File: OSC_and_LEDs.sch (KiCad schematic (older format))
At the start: 49 parts, among them Q2 IRLML2502, Q3 IRLML2502, Q4 IRLML2502, Q5 IRLML2502, Q6 IRLML2502, Q7 IRLML2502, U1 xc7a50tftg256, X1 ASFLMB

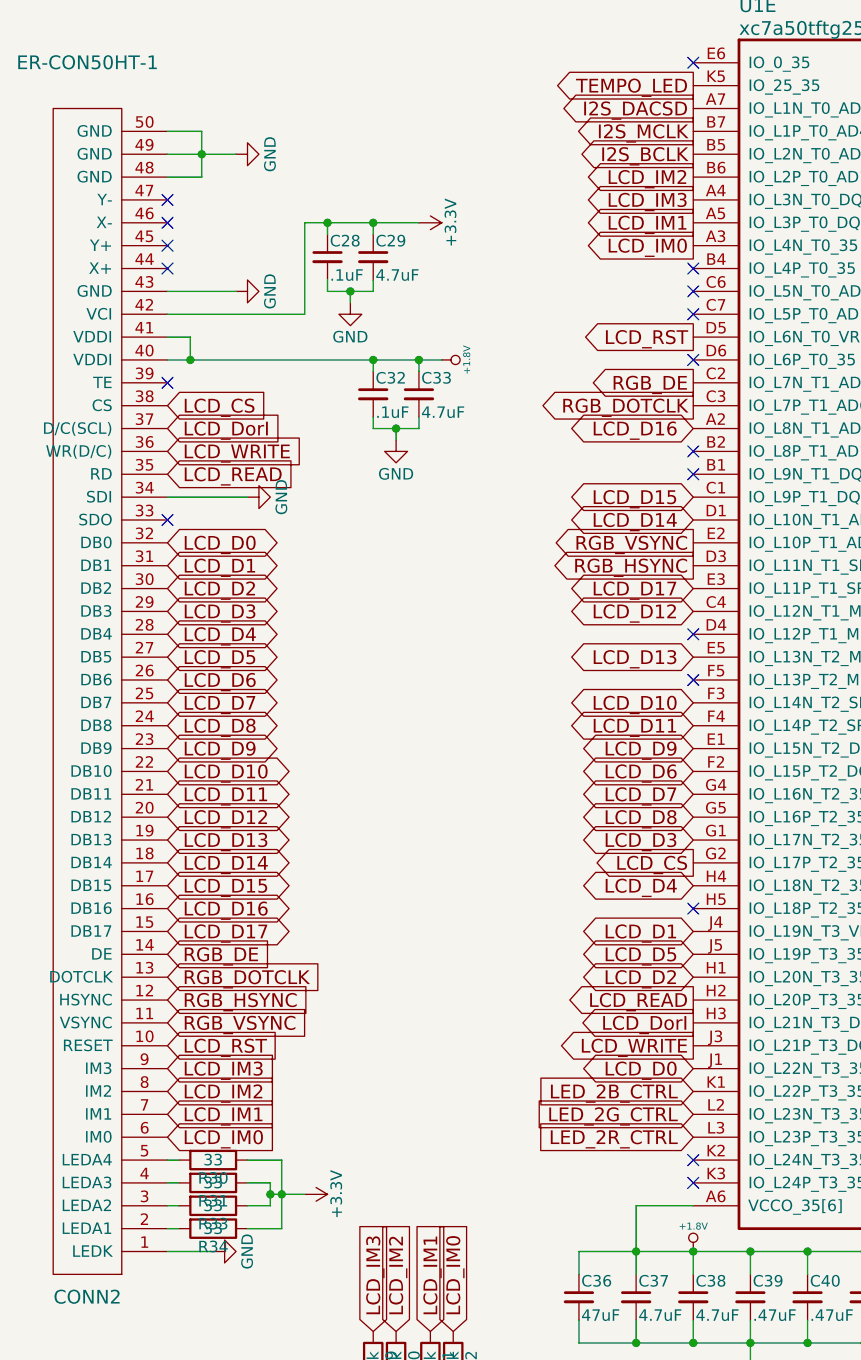
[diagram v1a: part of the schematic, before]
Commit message: all high speed busses added
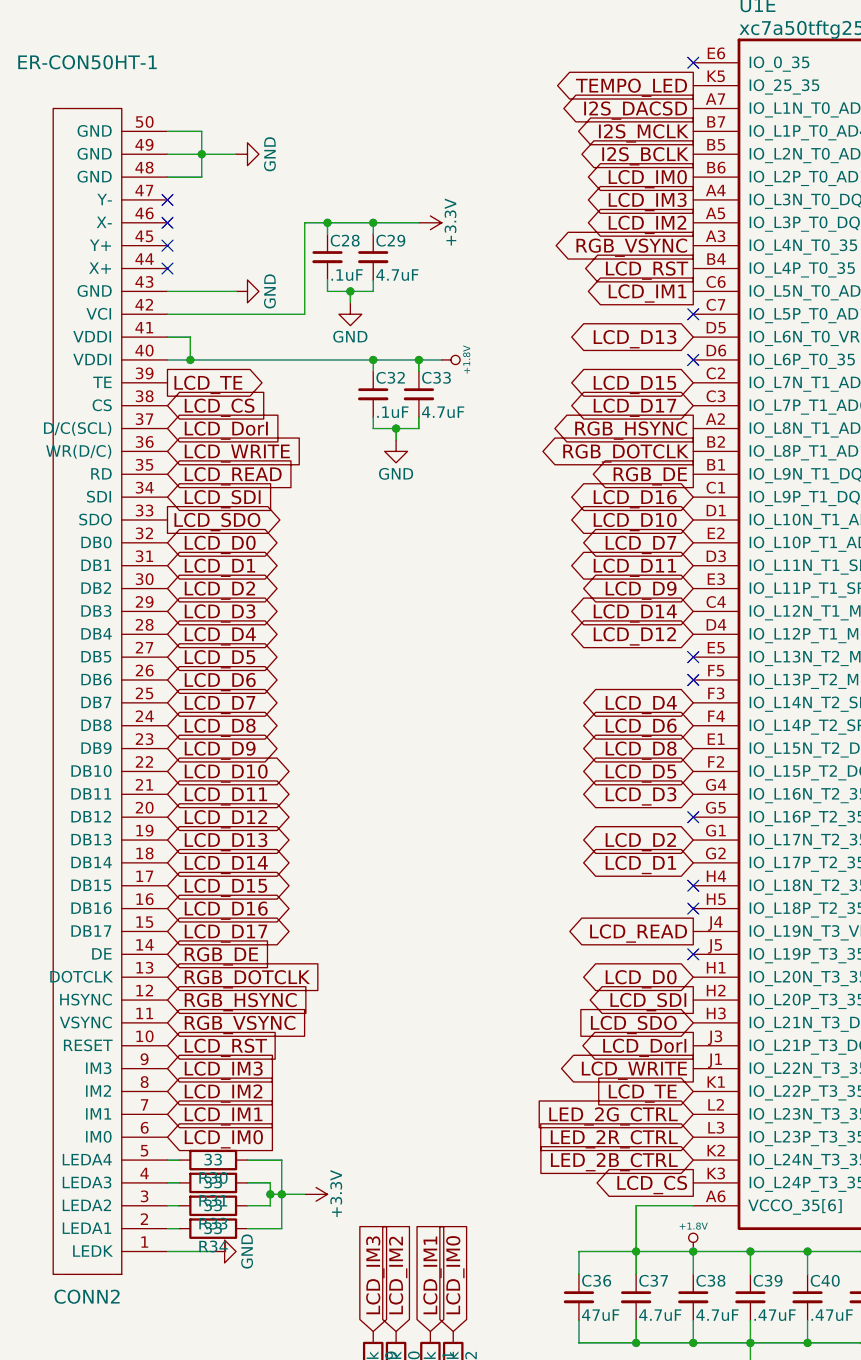
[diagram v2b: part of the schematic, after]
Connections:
- net GND: no longer CONN2.34 (SDI)
- net LCD_CS: now also U1.K3 (IO_L24P_T3_35); no longer U1.G2 (IO_L17P_T2_35)
- net LCD_D0: now also U1.H1 (IO_L20N_T3_35); no longer U1.J1 (IO_L22N_T3_35)
- net LCD_D1: now also U1.G2 (IO_L17P_T2_35); no longer U1.J4 (IO_L19N_T3_VREF_35)
- net LCD_D10: now also U1.D1 (IO_L10N_T1_AD15N_35); no longer U1.F3 (IO_L14N_T2_SRCC_35)
- net LCD_D11: now also U1.D3 (IO_L11N_T1_SRCC_35); no longer U1.F4 (IO_L14P_T2_SRCC_35)
- net LCD_D12: now also U1.D4 (IO_L12P_T1_MRCC_35); no longer U1.C4 (IO_L12N_T1_MRCC_35)
- net LCD_D13: now also U1.D5 (IO_L6N_T0_VREF_35); no longer U1.E5 (IO_L13N_T2_MRCC_35)
- net LCD_D14: now also U1.C4 (IO_L12N_T1_MRCC_35); no longer U1.D1 (IO_L10N_T1_AD15N_35)
- net LCD_D15: now also U1.C2 (IO_L7N_T1_AD6N_35); no longer U1.C1 (IO_L9P_T1_DQS_AD7P_35)
- net LCD_D16: now also U1.C1 (IO_L9P_T1_DQS_AD7P_35); no longer U1.A2 (IO_L8N_T1_AD14N_35)
- net LCD_D17: now also U1.C3 (IO_L7P_T1_AD6P_35); no longer U1.E3 (IO_L11P_T1_SRCC_35)
- net LCD_D2: now also U1.G1 (IO_L17N_T2_35); no longer U1.H1 (IO_L20N_T3_35)
- net LCD_D3: now also U1.G4 (IO_L16N_T2_35); no longer U1.G1 (IO_L17N_T2_35)
- net LCD_D4: now also U1.F3 (IO_L14N_T2_SRCC_35); no longer U1.H4 (IO_L18N_T2_35)
- net LCD_D5: now also U1.F2 (IO_L15P_T2_DQS_35); no longer U1.J5 (IO_L19P_T3_35)
- net LCD_D6: now also U1.F4 (IO_L14P_T2_SRCC_35); no longer U1.F2 (IO_L15P_T2_DQS_35)
- net LCD_D7: now also U1.E2 (IO_L10P_T1_AD15P_35); no longer U1.G4 (IO_L16N_T2_35)
- net LCD_D8: now also U1.E1 (IO_L15N_T2_DQS_35); no longer U1.G5 (IO_L16P_T2_35)
- net LCD_D9: now also U1.E3 (IO_L11P_T1_SRCC_35); no longer U1.E1 (IO_L15N_T2_DQS_35)
- net LCD_DorI: now also U1.J3 (IO_L21P_T3_DQS_35); no longer U1.H3 (IO_L21N_T3_DQS_35)
- net LCD_IM0: now also U1.B6 (IO_L2P_T0_AD12P_35); no longer U1.A3 (IO_L4N_T0_35)
- net LCD_IM1: now also U1.C6 (IO_L5N_T0_AD13N_35); no longer U1.A5 (IO_L3P_T0_DQS_AD5P_35)
- net LCD_IM2: now also U1.A5 (IO_L3P_T0_DQS_AD5P_35); no longer U1.B6 (IO_L2P_T0_AD12P_35)
- net LCD_READ: now also U1.J4 (IO_L19N_T3_VREF_35); no longer U1.H2 (IO_L20P_T3_35)
- net LCD_RST: now also U1.B4 (IO_L4P_T0_35); no longer U1.D5 (IO_L6N_T0_VREF_35)
- net LCD_WRITE: now also U1.J1 (IO_L22N_T3_35); no longer U1.J3 (IO_L21P_T3_DQS_35)
- net LED_2B_CTRL: now also U1.K2 (IO_L24N_T3_35); no longer U1.K1 (IO_L22P_T3_35)
- net RGB_DE: now also U1.B1 (IO_L9N_T1_DQS_AD7N_35); no longer U1.C2 (IO_L7N_T1_AD6N_35)
- net RGB_DOTCLK: now also U1.B2 (IO_L8P_T1_AD14P_35); no longer U1.C3 (IO_L7P_T1_AD6P_35)
- net RGB_HSYNC: now also U1.A2 (IO_L8N_T1_AD14N_35); no longer U1.D3 (IO_L11N_T1_SRCC_35)
- net RGB_VSYNC: now also U1.A3 (IO_L4N_T0_35); no longer U1.E2 (IO_L10P_T1_AD15P_35)
- net LCD_SDO: now reaches CONN2.33 (SDO)
- net LCD_SDO: now also U1.H3 (IO_L21N_T3_DQS_35)
- net LCD_TE: now reaches CONN2.39 (TE)
- net LCD_TE: now also U1.K1 (IO_L22P_T3_35)
- new net LCD_SDI: CONN2.34 (SDI), U1.H2 (IO_L20P_T3_35)
- no-connect marks 30 -> 25
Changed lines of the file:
@@
-$EndComp
-$Comp
-L GND #PWR053
-U 1 1 598D5E39
-P 7650 2800
-F 0 "#PWR053" H 7650 2550 50  0001 C CNN
-F 1 "GND" H 7650 2650 50  0000 C CNN
-F 2 "" H 7650 2800 50  0000 C CNN
-F 3 "" H 7650 2800 50  0000 C CNN
-	1    7650 2800
-	0    -1   -1   0
 $EndComp
 $Comp
@@
 $EndComp
 $Comp
-L GND #PWR054
+L GND #PWR053
 U 1 1 598F040F
 P 4750 1600
-F 0 "#PWR054" H 4750 1350 50  0001 C CNN
+F 0 "#PWR053" H 4750 1350 50  0001 C CNN
 F 1 "GND" H 4750 1450 50  0000 C CNN
 F 2 "" H 4750 1600 50  0000 C CNN
@@
 $EndComp
 $Comp
-L +3.3V #PWR055
+L +3.3V #PWR054
 U 1 1 598F1F44
 P 4300 2100
-F 0 "#PWR055" H 4300 1950 50  0001 C CNN
+F 0 "#PWR054" H 4300 1950 50  0001 C CNN
 F 1 "+3.3V" H 4300 2240 50  0000 C CNN
 F 2 "" H 4300 2100 50  0000 C CNN
@@
 $EndComp
 $Comp
-L GND #PWR056
+L GND #PWR055
 U 1 1 598FDD2A
 P 4500 2600
-F 0 "#PWR056" H 4500 2350 50  0001 C CNN
+F 0 "#PWR055" H 4500 2350 50  0001 C CNN
 F 1 "GND" H 4500 2450 50  0000 C CNN
 F 2 "" H 4500 2600 50  0000 C CNN
@@
 $EndComp
 $Comp
-L GND #PWR057
+L GND #PWR056
 U 1 1 598D6E85
 P 2550 4500
-F 0 "#PWR057" H 2550 4250 50  0001 C CNN
+F 0 "#PWR056" H 2550 4250 50  0001 C CNN
 F 1 "GND" H 2550 4350 50  0000 C CNN
 F 2 "" H 2550 4500 50  0000 C CNN
@@
 $EndComp
 $Comp
-L GND #PWR058
+L GND #PWR057
 U 1 1 598D6E8B
 P 2550 4000
-F 0 "#PWR058" H 2550 3750 50  0001 C CNN
+F 0 "#PWR057" H 2550 3750 50  0001 C CNN
 F 1 "GND" H 2550 3850 50  0000 C CNN
 F 2 "" H 2550 4000 50  0000 C CNN
@@
 $EndComp
 $Comp
-L GND #PWR059
+L GND #PWR058
 U 1 1 598D6E97
 P 2550 3700
-F 0 "#PWR059" H 2550 3450 50  0001 C CNN
+F 0 "#PWR058" H 2550 3450 50  0001 C CNN
 F 1 "GND" H 2550 3550 50  0000 C CNN
 F 2 "" H 2550 3700 50  0000 C CNN
@@
 $EndComp
 $Comp
-L GND #PWR060
+L GND #PWR059
 U 1 1 598D6E9D
 P 2550 3600
-F 0 "#PWR060" H 2550 3350 50  0001 C CNN
+F 0 "#PWR059" H 2550 3350 50  0001 C CNN
 F 1 "GND" H 2550 3450 50  0000 C CNN
 F 2 "" H 2550 3600 50  0000 C CNN
@@
 $EndComp
 $Comp
-L GND #PWR061
+L GND #PWR060
 U 1 1 598D6EA3
 P 2550 3300
-F 0 "#PWR061" H 2550 3050 50  0001 C CNN
+F 0 "#PWR060" H 2550 3050 50  0001 C CNN
 F 1 "GND" H 2550 3150 50  0000 C CNN
 F 2 "" H 2550 3300 50  0000 C CNN
@@
 $EndComp
 $Comp
-L GND #PWR062
+L GND #PWR061
 U 1 1 598D6EA9
 P 2550 3000
-F 0 "#PWR062" H 2550 2750 50  0001 C CNN
+F 0 "#PWR061" H 2550 2750 50  0001 C CNN
 F 1 "GND" H 2550 2850 50  0000 C CNN
 F 2 "" H 2550 3000 50  0000 C CNN
@@
 $EndComp
 $Comp
-L GND #PWR063
+L GND #PWR062
 U 1 1 598D6EAF
 P 2550 2700
-F 0 "#PWR063" H 2550 2450 50  0001 C CNN
+F 0 "#PWR062" H 2550 2450 50  0001 C CNN
 F 1 "GND" H 2550 2550 50  0000 C CNN
 F 2 "" H 2550 2700 50  0000 C CNN
@@
 $EndComp
 $Comp
-L GND #PWR064
+L GND #PWR063
 U 1 1 598D6EB7
 P 2550 2800
-F 0 "#PWR064" H 2550 2550 50  0001 C CNN
+F 0 "#PWR063" H 2550 2550 50  0001 C CNN
 F 1 "GND" H 2550 2650 50  0000 C CNN
 F 2 "" H 2550 2800 50  0000 C CNN
@@
 $EndComp
 $Comp
-L +1.8V #PWR065
+L +1.8V #PWR064
 U 1 1 598CFD34
 P 8500 6900
-F 0 "#PWR065" H 8500 7040 20  0001 C CNN
+F 0 "#PWR064" H 8500 7040 20  0001 C CNN
 F 1 "+1.8V" H 8500 7010 30  0000 C CNN
 F 2 "" H 8500 6900 60  0001 C CNN
@@
 $EndComp
 $Comp
-L GND #PWR066
+L GND #PWR065
 U 1 1 598D049B
 P 8250 6900
-F 0 "#PWR066" H 8250 6650 50  0001 C CNN
+F 0 "#PWR065" H 8250 6650 50  0001 C CNN
 F 1 "GND" H 8250 6750 50  0000 C CNN
 F 2 "" H 8250 6900 50  0000 C CNN
@@
 Text GLabel 7300 2400 2    60   Input ~ 0
 LCD_CS
-Text GLabel 9600 5300 0    60   BiDi ~ 0
-LCD_D0
-Text GLabel 9600 4700 0    60   BiDi ~ 0
+Text GLabel 9600 4400 0    60   BiDi ~ 0
 LCD_D1
-Text GLabel 9600 4900 0    60   BiDi ~ 0
+Text GLabel 9600 4300 0    60   BiDi ~ 0
 LCD_D2
-Text GLabel 9600 4300 0    60   BiDi ~ 0
-LCD_D3
-Text GLabel 9600 4500 0    60   BiDi ~ 0
+Text GLabel 9600 3700 0    60   BiDi ~ 0
 LCD_D4
-Text GLabel 9600 4800 0    60   BiDi ~ 0
+Text GLabel 9600 4000 0    60   BiDi ~ 0
 LCD_D5
-Text GLabel 9600 4000 0    60   BiDi ~ 0
-LCD_D6
-Text GLabel 9600 4100 0    60   BiDi ~ 0
-LCD_D7
-Text GLabel 9600 4200 0    60   BiDi ~ 0
-LCD_D8
-Text GLabel 9600 3900 0    60   BiDi ~ 0
-LCD_D9
-Text GLabel 9600 3700 0    60   BiDi ~ 0
-LCD_D10
-Text GLabel 9600 3800 0    60   BiDi ~ 0
-LCD_D11
-Text GLabel 9600 3300 0    60   BiDi ~ 0
-LCD_D12
-Text GLabel 9600 3500 0    60   BiDi ~ 0
-LCD_D13
-Text GLabel 9600 2900 0    60   BiDi ~ 0
-LCD_D14
-Text GLabel 9600 2800 0    60   BiDi ~ 0
+Text GLabel 9600 2300 0    60   BiDi ~ 0
 LCD_D15
-Text GLabel 9600 2500 0    60   BiDi ~ 0
-LCD_D16
-Text GLabel 9600 3200 0    60   BiDi ~ 0
-LCD_D17
-Text GLabel 9600 5000 0    60   Output ~ 0
+Text GLabel 9600 4700 0    60   Output ~ 0
 LCD_READ
 Text GLabel 9600 5200 0    60   Output ~ 0
-LCD_WRITE
-Text GLabel 9600 5100 0    60   Output ~ 0
 LCD_DorI
-Text GLabel 9600 4400 0    60   Output ~ 0
+Text GLabel 9600 5800 0    60   Output ~ 0
 LCD_CS
-Text GLabel 9600 2300 0    60   Output ~ 0
-RGB_DE
-Text GLabel 9600 2400 0    60   Output ~ 0
+Text GLabel 9600 2600 0    60   Output ~ 0
 RGB_DOTCLK
-Text GLabel 9600 3100 0    60   Output ~ 0
-RGB_HSYNC
-Text GLabel 9600 3000 0    60   Output ~ 0
-RGB_VSYNC
-Text GLabel 9600 2100 0    60   Output ~ 0
+Text GLabel 9600 1800 0    60   Output ~ 0
 LCD_RST
 Text GLabel 4950 1900 0    60   Input ~ 0
@@
 Text GLabel 9600 5500 0    60   Input ~ 0
 LED_2G_CTRL
-Text GLabel 9600 5400 0    60   Input ~ 0
+Text GLabel 9600 5700 0    60   Input ~ 0
 LED_2B_CTRL
 Text GLabel 8200 6450 1    60   Input ~ 0
@@
 Text GLabel 9600 1500 0    60   Output ~ 0
 LCD_IM3
+Text GLabel 9600 1600 0    60   Output ~ 0
+LCD_IM2
+Text GLabel 9600 1900 0    60   Output ~ 0
+LCD_IM1
 Text GLabel 9600 1400 0    60   Output ~ 0
-LCD_IM2
-Text GLabel 9600 1600 0    60   Output ~ 0
-LCD_IM1
-Text GLabel 9600 1700 0    60   Output ~ 0
 LCD_IM0
 Wire Wire Line
@@
 Wire Wire Line
 	7750 5900 7750 5800
-Wire Wire Line
-	7650 2800 7300 2800
 Wire Wire Line
 	4750 1600 4950 1600
@@
 Connection ~ 8500 6900
 Connection ~ 8250 6900
-NoConn ~ 7300 2900
-NoConn ~ 7300 2300
-NoConn ~ 9600 4600
 NoConn ~ 7300 1500
 NoConn ~ 7300 1600
@@
 NoConn ~ 2550 2900
 NoConn ~ 9600 900
-NoConn ~ 9600 1800
-NoConn ~ 9600 1900
-NoConn ~ 9600 2000
-NoConn ~ 9600 2600
 NoConn ~ 9600 3600
 $Comp
@@
 	0    1    1    0
 $EndComp
-NoConn ~ 9600 2700
-$Comp
-L GND #PWR067
+$Comp
+L GND #PWR066
 U 1 1 5A746D29
 P 2550 4600
-F 0 "#PWR067" H 2550 4350 50  0001 C CNN
+F 0 "#PWR066" H 2550 4350 50  0001 C CNN
 F 1 "GND" H 2550 4450 50  0000 C CNN
 F 2 "" H 2550 4600 50  0000 C CNN
@@
 NoConn ~ 2550 4100
 NoConn ~ 2550 3900
-NoConn ~ 9600 3400
 Text GLabel 9600 1100 0    60   Output ~ 0
 I2S_DACSD
 Text GLabel 9600 1200 0    60   Output ~ 0
 I2S_MCLK
+NoConn ~ 9600 4200
+NoConn ~ 9600 3500
+NoConn ~ 9600 4800
+Text GLabel 7300 2300 2    60   Output ~ 0
+LCD_TE
+Text GLabel 7300 2900 2    60   Output ~ 0
+LCD_SDO
+Text GLabel 7300 2800 2    60   Input ~ 0
+LCD_SDI
 $Comp
 L xc7a50tftg256 U?
@@
 	1    0    0    -1
 $EndComp
+NoConn ~ 9600 2000
 NoConn ~ 9600 2200
-NoConn ~ 9600 5700
-NoConn ~ 9600 5800
+NoConn ~ 9600 4500
+NoConn ~ 9600 4600
+Text GLabel 9600 1700 0    60   Output ~ 0
+RGB_VSYNC
+Text GLabel 9600 2500 0    60   Output ~ 0
+RGB_HSYNC
+Text GLabel 9600 2700 0    60   Output ~ 0
+RGB_DE
+Text GLabel 9600 2400 0    60   BiDi ~ 0
+LCD_D17
+Text GLabel 9600 3300 0    60   BiDi ~ 0
+LCD_D14
+Text GLabel 9600 3400 0    60   BiDi ~ 0
+LCD_D12
+Text GLabel 9600 2100 0    60   BiDi ~ 0
+LCD_D13
+Text GLabel 9600 3100 0    60   BiDi ~ 0
+LCD_D11
+Text GLabel 9600 2900 0    60   BiDi ~ 0
+LCD_D10
+Text GLabel 9600 2800 0    60   BiDi ~ 0
+LCD_D16
+Text GLabel 9600 3200 0    60   BiDi ~ 0
+LCD_D9
+Text GLabel 9600 3900 0    60   BiDi ~ 0
+LCD_D8
+Text GLabel 9600 3000 0    60   BiDi ~ 0
+LCD_D7
+Text GLabel 9600 3800 0    60   BiDi ~ 0
+LCD_D6
+Text GLabel 9600 4100 0    60   BiDi ~ 0
+LCD_D3
+Text GLabel 9600 4900 0    60   BiDi ~ 0
+LCD_D0
+Text GLabel 9600 5100 0    60   Input ~ 0
+LCD_SDO
+Text GLabel 9600 5000 0    60   Output ~ 0
+LCD_SDI
+Text GLabel 9600 5300 0    60   Output ~ 0
+LCD_WRITE
+Text GLabel 9600 5400 0    60   Input ~ 0
+LCD_TE
 $EndSCHEMATC
